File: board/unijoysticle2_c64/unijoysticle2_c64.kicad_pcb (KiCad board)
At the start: 4 copper layers, 62.5 x 60 mm, 62 parts, among them J1 USB_B_Micro, J2 PORT JOY #1, J3 PORT JOY #2, Q1 S8050, Q2 S8050, SW1 RESET, SW2 BOOT, SW3 MODE, SW4 SWAP, U1 ESP32-WROOM-32E, U2 AMS1117-3.3, U3 CH340C, U4 74HC05, U5 74HC05, U6 74HC05

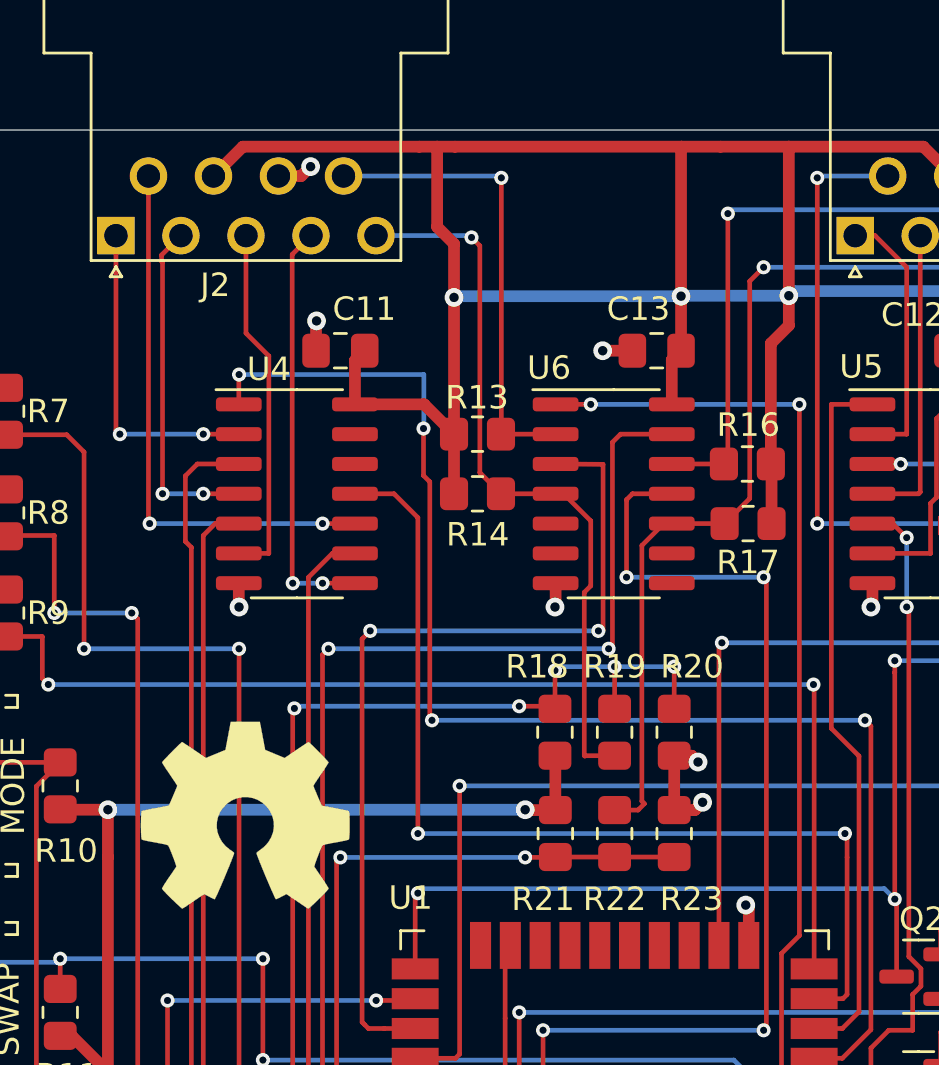
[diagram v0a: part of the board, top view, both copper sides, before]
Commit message: c64: rev B
Rev A had conflict with SYNC and 2nd and 3rd buttons
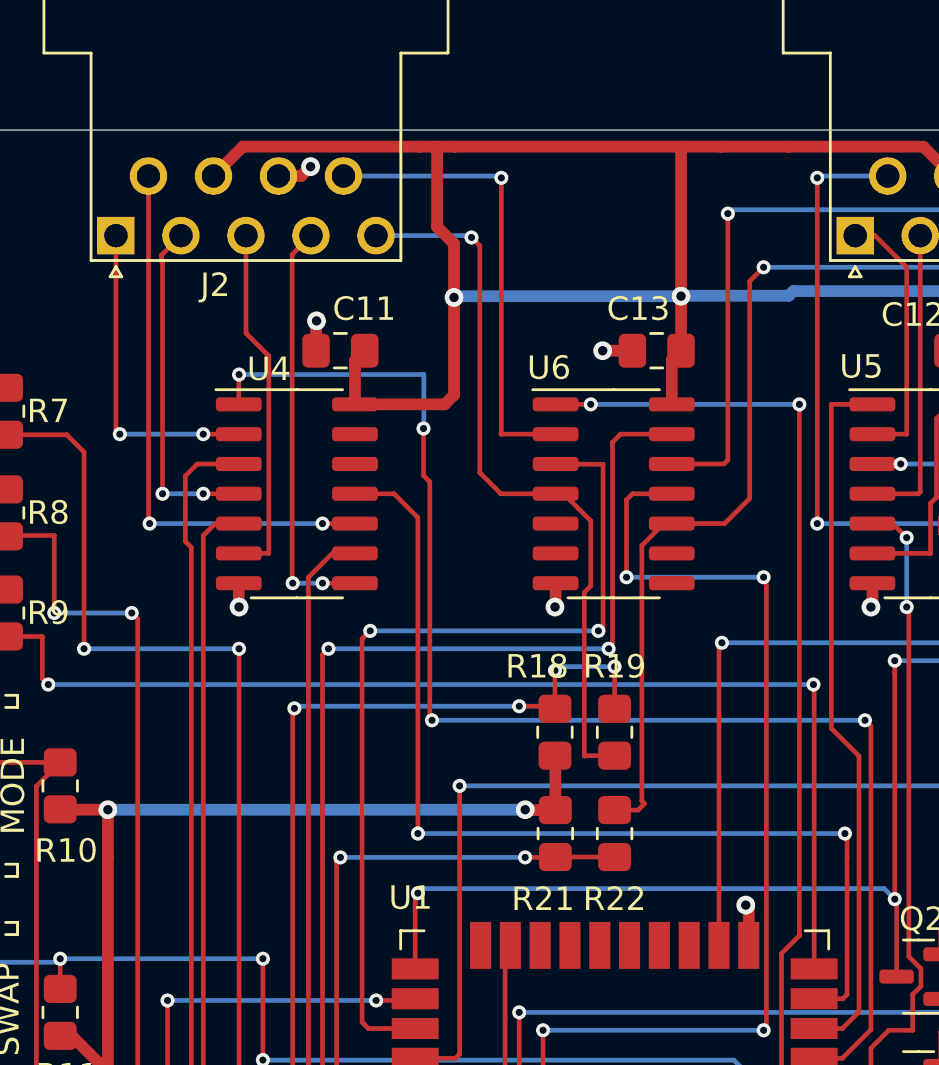
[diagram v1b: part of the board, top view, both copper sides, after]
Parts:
- removed R13, R14, R16, R17: 8.2K, Resistor_SMD:R_0805_2012Metric_Pad1.20x1.40mm_HandSolder
- removed R20, R23: 3.3K, Resistor_SMD:R_0805_2012Metric_Pad1.20x1.40mm_HandSolder
- removed REF**: OSHW-Symbol_8.9x8mm_SilkScreen, Symbol:OSHW-Symbol_8.9x8mm_SilkScreen
- R19, R22: value 1.7K -> 150
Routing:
- net +5V: track 117.7 -> 96.7 mm, vias 5 -> 4
- net GND: track 72.9 -> 68.1 mm, vias 35 -> 33
- net GPIO_36: track 67.4 -> 63.0 mm, vias 7 -> 6
- net GPIO_39: track 49.5 -> 47.0 mm
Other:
- board text added: "Unijoysticle 2 C64 Rev. B"
- board text removed: "Unijoysticle 2 C64 Rev. A"

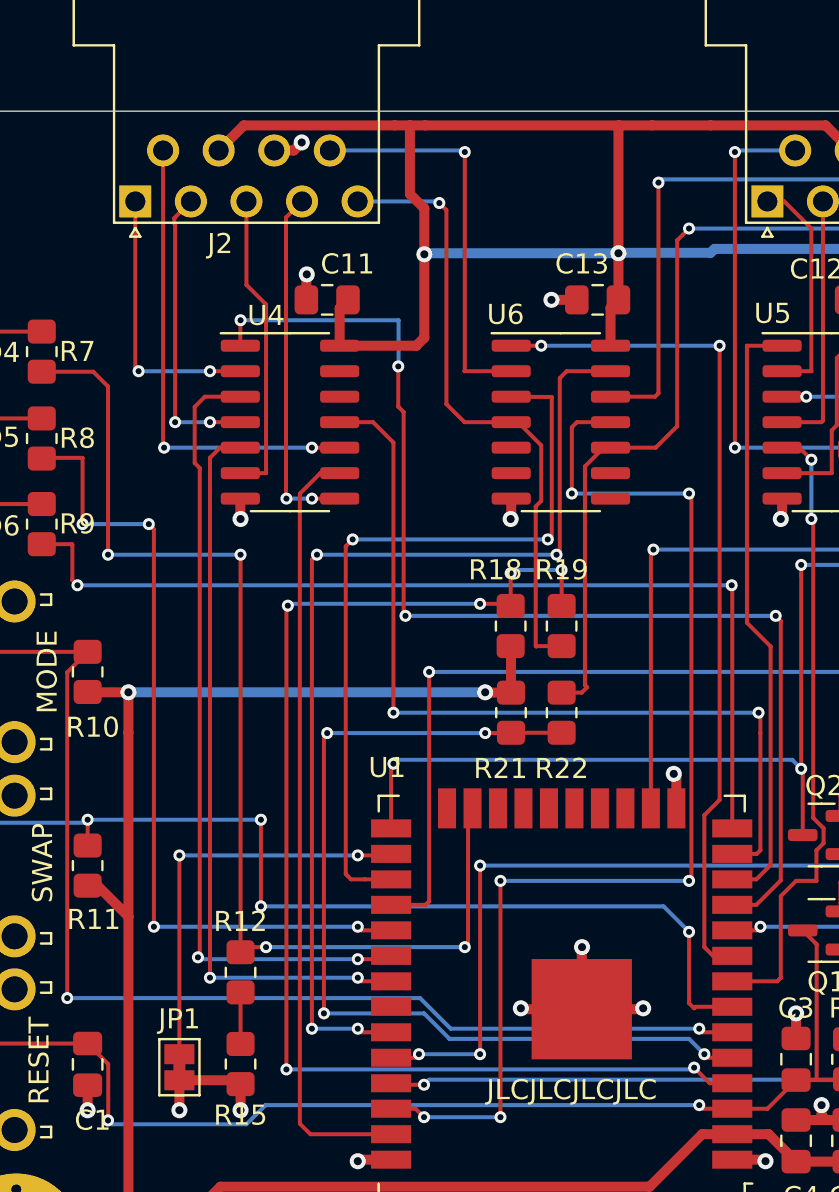
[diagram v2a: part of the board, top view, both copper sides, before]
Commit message: Unijoysticle C64 rev C
It is like A, with simplified sync circuit:
 - removed pull-down and pull-up resistor from SYNC

Seems to be working Ok.
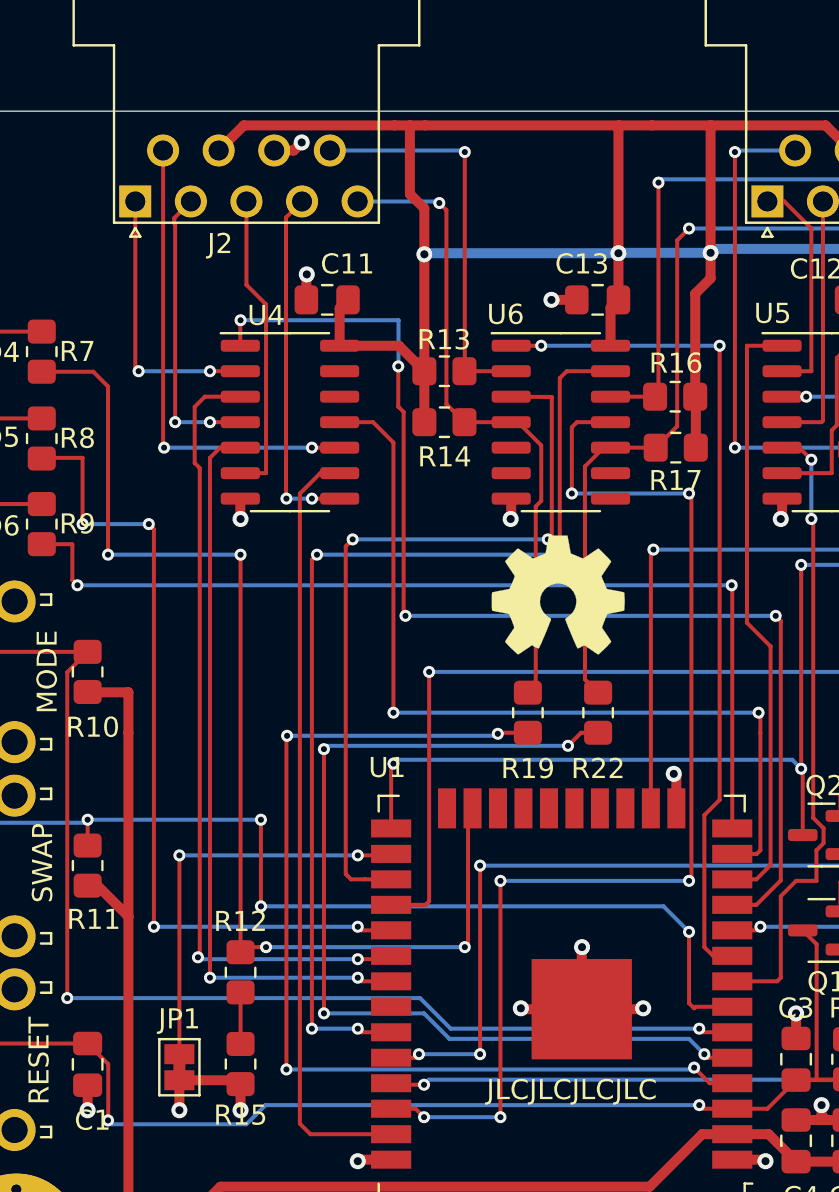
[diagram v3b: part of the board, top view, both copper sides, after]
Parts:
- removed R18, R21: 10K, Resistor_SMD:R_0805_2012Metric_Pad1.20x1.40mm_HandSolder
- added R13: 8.2K, Resistor_SMD:R_0805_2012Metric_Pad1.20x1.40mm_HandSolder, F.Cu at (107.7, 103.0)
- added R14: 8.2K, Resistor_SMD:R_0805_2012Metric_Pad1.20x1.40mm_HandSolder, F.Cu at (107.7, 105.5)
- added R16: 8.2K, Resistor_SMD:R_0805_2012Metric_Pad1.20x1.40mm_HandSolder, F.Cu at (119.2, 104.2)
- added R17: 8.2K, Resistor_SMD:R_0805_2012Metric_Pad1.20x1.40mm_HandSolder, F.Cu at (119.2, 106.8)
- added REF**: OSHW-Symbol_6.7x6mm_SilkScreen, Symbol:OSHW-Symbol_6.7x6mm_SilkScreen, F.Cu at (113.3, 114.1)
- R19, R22: value 150 -> 1.7K
- moved R19 4.63 mm to (111.8, 120.0), turned to -90 degrees
- moved R22 1.82 mm to (115.3, 120.0)
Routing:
- net +3V3: track 138.3 -> 116.9 mm, vias 8 -> 6
- net +5V: track 96.7 -> 117.7 mm, vias 4 -> 5
- net GPIO_36: track 63.0 -> 51.4 mm, vias 6 -> 4
- net GPIO_39: track 47.0 -> 48.4 mm
- net /C64 Ports/J1_POTY: track 31.3 -> 32.4 mm
- net /C64 Ports/J2_POTY: track 43.5 -> 42.6 mm
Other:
- board text added: "Unijoysticle 2 C64 Rev. C"
- board text added: "©️ 2023 Ricardo Quesada http://retro.moe"
- board text removed: "Unijoysticle 2 C64 Rev. B"
- board text removed: "©️ 2022 Ricardo Quesada http://retro.moe"

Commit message: C64: Update resistor values for Pull ups and SYNC
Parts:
- R12, R7, R8, R9: value 3.3K -> 3K3
- R13, R14, R16, R17: value 8.2K -> 2K7
- R19, R22: value 1.7K -> 1K7
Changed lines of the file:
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@@
       (effects (font (size 1 1) (thickness 0.15)))
     )
-    (fp_text value "3.3K" (at 0 1.65 90) (layer "F.Fab")
+    (fp_text value "3K3" (at 0 1.65 90) (layer "F.Fab")
       (effects (font (size 1 1) (thickness 0.15)))
     )
@@
       (effects (font (size 1 1) (thickness 0.15)))
     )
-    (fp_text value "8.2K" (at 0 1.65) (layer "F.Fab")
+    (fp_text value "2K7" (at 0 1.65) (layer "F.Fab")
       (effects (font (size 1 1) (thickness 0.15)))
     )
@@
       (effects (font (size 1 1) (thickness 0.15)))
     )
-    (fp_text value "8.2K" (at 0 1.65) (layer "F.Fab")
+    (fp_text value "2K7" (at 0 1.65) (layer "F.Fab")
       (effects (font (size 1 1) (thickness 0.15)))
     )
@@
       (effects (font (size 1 1) (thickness 0.15)))
     )
-    (fp_text value "3.3K" (at 0 1.65 90) (layer "F.Fab")
+    (fp_text value "3K3" (at 0 1.65 90) (layer "F.Fab")
       (effects (font (size 1 1) (thickness 0.15)))
     )
@@
       (effects (font (size 1 1) (thickness 0.15)))
     )
-    (fp_text value "8.2K" (at 0 1.65) (layer "F.Fab")
+    (fp_text value "2K7" (at 0 1.65) (layer "F.Fab")
       (effects (font (size 1 1) (thickness 0.15)))
     )
@@
       (effects (font (size 1 1) (thickness 0.15)))
     )
-    (fp_text value "3.3K" (at 0 1.65 90) (layer "F.Fab")
+    (fp_text value "3K3" (at 0 1.65 90) (layer "F.Fab")
       (effects (font (size 1 1) (thickness 0.15)))
     )
@@
       (effects (font (size 1 1) (thickness 0.15)))
     )
-    (fp_text value "3.3K" (at 0 1.65 90) (layer "F.Fab")
+    (fp_text value "3K3" (at 0 1.65 90) (layer "F.Fab")
       (effects (font (size 1 1) (thickness 0.15)))
     )
@@
       (effects (font (size 1 1) (thickness 0.15)))
     )
-    (fp_text value "8.2K" (at 0 1.65) (layer "F.Fab")
+    (fp_text value "2K7" (at 0 1.65) (layer "F.Fab")
       (effects (font (size 1 1) (thickness 0.15)))
     )
@@
       (effects (font (size 1 1) (thickness 0.15)))
     )
-    (fp_text value "1.7K" (at 0 1.65 90) (layer "F.Fab")
+    (fp_text value "1K7" (at 0 1.65 90) (layer "F.Fab")
       (effects (font (size 1 1) (thickness 0.15)))
     )
@@
       (effects (font (size 1 1) (thickness 0.15)))
     )
-    (fp_text value "1.7K" (at 0 1.65 90) (layer "F.Fab")
-      (effects (font (size 1 1) (thickness 0.15)))
-    )
+    (fp_text value "1K7" (at 0 1.65 90) (layer "F.Fab")
+      (effects (font (size 1 1) (thickness 0.15)))
+    )

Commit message: Unijoysticle C64: Rev C
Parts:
- R19, R22: value 1K7 -> 6K8
- R2: value 3.3K -> 3K3
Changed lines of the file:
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@@
       (drillshape 0)
       (scaleselection 1)
-      (outputdirectory "gerber_a/")
+      (outputdirectory "assembly_c/")
     )
   )
@@
       (effects (font (size 1 1) (thickness 0.15)))
     )
-    (fp_text value "3.3K" (at 0 1.65) (layer "F.Fab")
+    (fp_text value "3K3" (at 0 1.65) (layer "F.Fab")
       (effects (font (size 1 1) (thickness 0.15)))
     )
@@
       (effects (font (size 1 1) (thickness 0.15)))
     )
-    (fp_text value "1K7" (at 0 1.65 90) (layer "F.Fab")
+    (fp_text value "6K8" (at 0 1.65 90) (layer "F.Fab")
       (effects (font (size 1 1) (thickness 0.15)))
     )
@@
       (effects (font (size 1 1) (thickness 0.15)))
     )
-    (fp_text value "1K7" (at 0 1.65 90) (layer "F.Fab")
-      (effects (font (size 1 1) (thickness 0.15)))
-    )
+    (fp_text value "6K8" (at 0 1.65 90) (layer "F.Fab")
+      (effects (font (size 1 1) (thickness 0.15)))
+    )
